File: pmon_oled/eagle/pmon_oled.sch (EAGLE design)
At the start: 37 parts, among them J1 USB, J2 USB, J4 PINHD-1X3, J5 PINHD-2X3, Q1 16Mhz, U1 LTC2943, U2 FT232RL, U3 LT1764AEQ, U4 ATMEGA328TQFP32

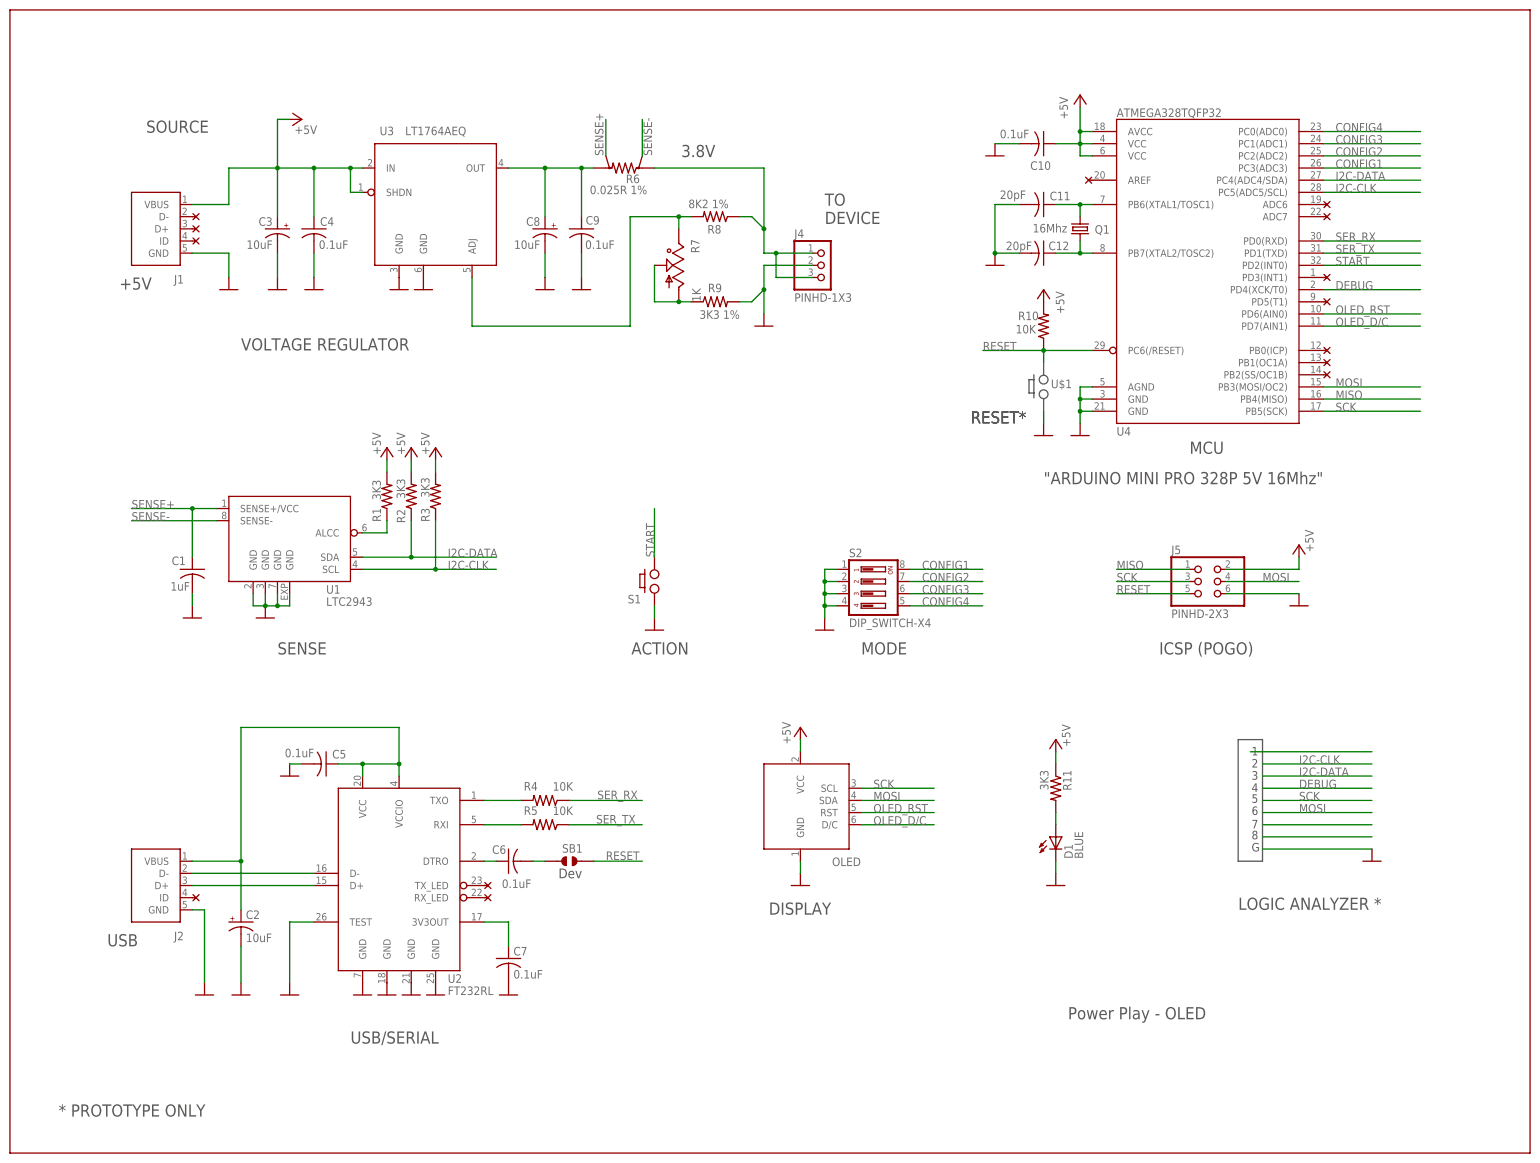
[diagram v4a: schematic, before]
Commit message: Redesigned the OLED board to pass 5V through rather than regulating to 3.8. This way it can be sued with non instrumeted devices, feeding to the USB input (with some reduce accuracy due to charger standby current and device behavior triggered by the charger in status).
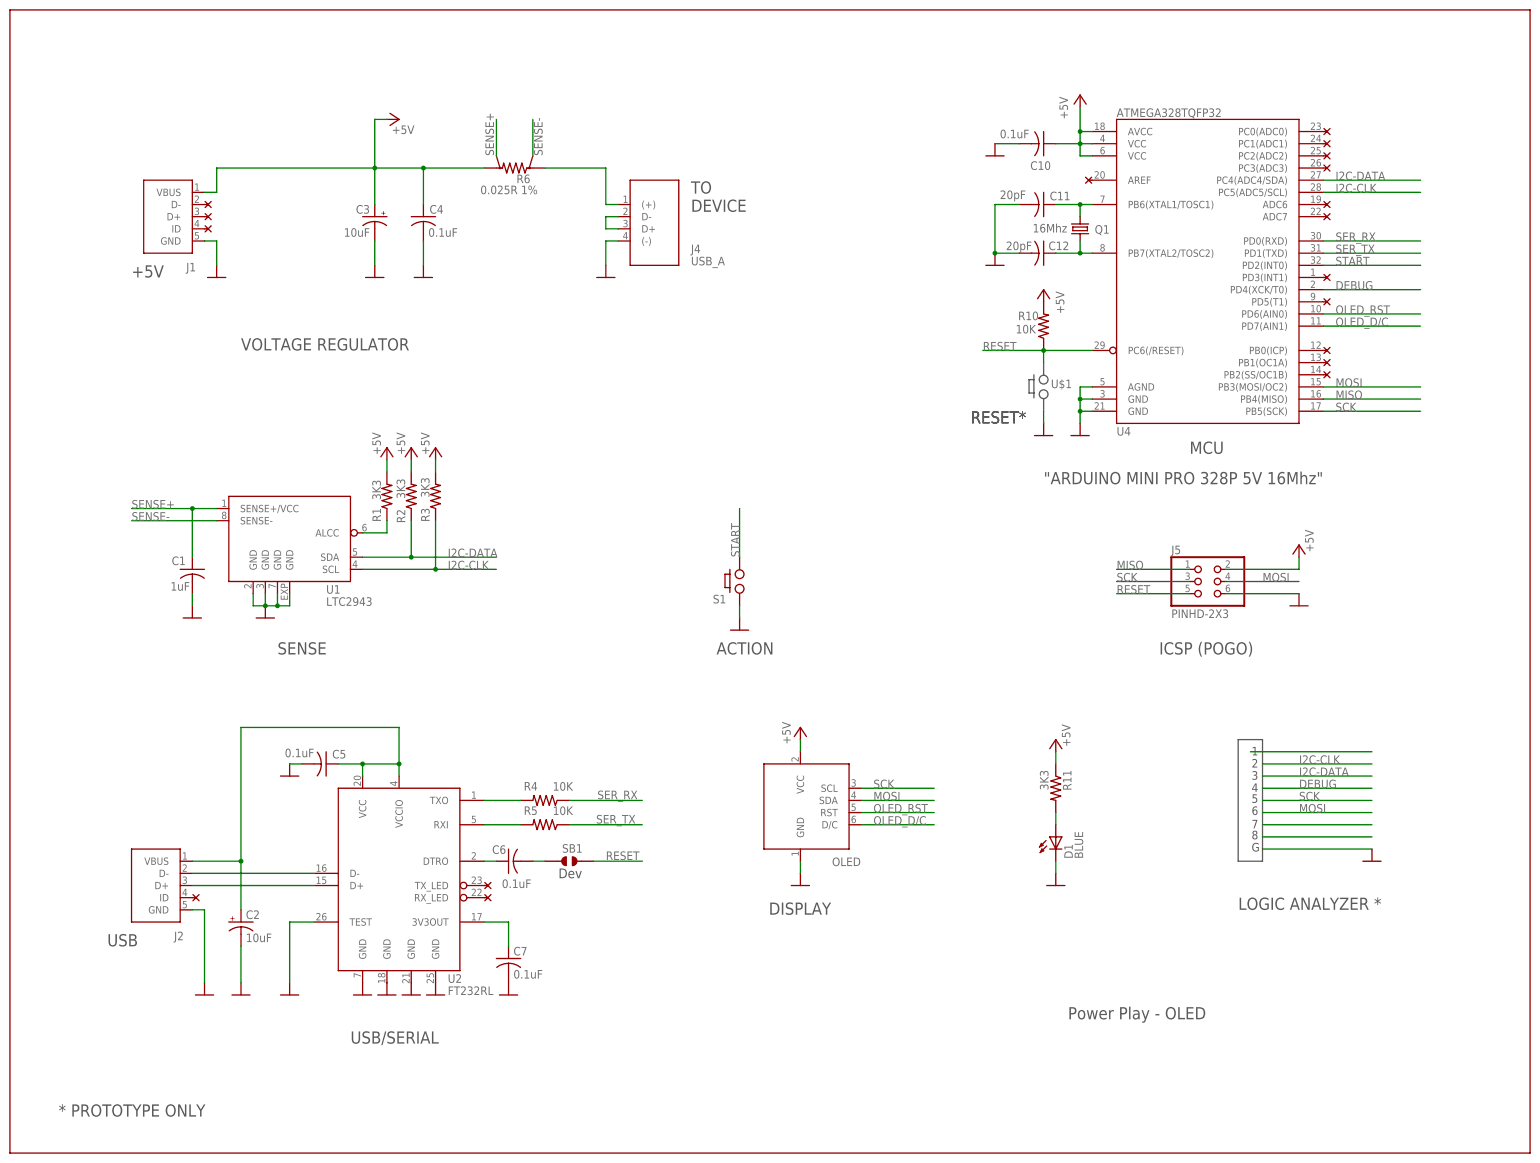
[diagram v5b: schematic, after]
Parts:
- removed C8: 10uF, pmon_oled:CPOL-USA/3216-18R
- removed C9: 0.1uF, pmon_oled:CAP-C0603
- removed R7: 1K, pmon_oled:TRIM_US-SM-42/43A
- removed R8: 8K2 1%, pmon_oled:RES-R0603
- removed R9: 3K3 1%, pmon_oled:RES-R0603
- removed S2: DIP_SWITCH-X4, pmon_oled:DIP_SWITCH-X4
- removed U3: LT1764AEQ, pmon_oled:LTE1764
- J4: value PINHD-1X3 -> USB_A; device pmon_oled:PINHD-1X3 -> pmon_oled:USB_A
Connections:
- removed net CONFIG1: S2.8, U4.PC3(ADC3)
- removed net CONFIG2: S2.7, U4.PC2(ADC2)
- removed net CONFIG3: S2.6, U4.PC1(ADC1)
- removed net CONFIG4: S2.5, U4.PC0(ADC0)
- removed net N$18: R7.1, R7.2, R9.1
- removed net N$19: R7.3, R8.2, U3.ADJ
- removed net N$9: C8.+, C9.1, R6.I2, U3.OUT
- new net N$4: J4.D+, J4.D-
- net +5V: now also R6.I2; no longer U3.IN, U3.SHDN
- net GND: now also J4.(-); no longer C8.-, C9.2, J4.2, R9.2, S2.1, S2.2, S2.3, S2.4, U3.GND@1, U3.GND@2
- net N$22: now also J4.(+); no longer J4.1, J4.3, R8.1
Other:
- note removed: "3.8V"
- note removed: "MODE"
- note removed: "SOURCE"
- moved on the sheet: C3, C4, J1, R6, S1

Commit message: Restoring the pmon_oled design with 3.8V regulator.
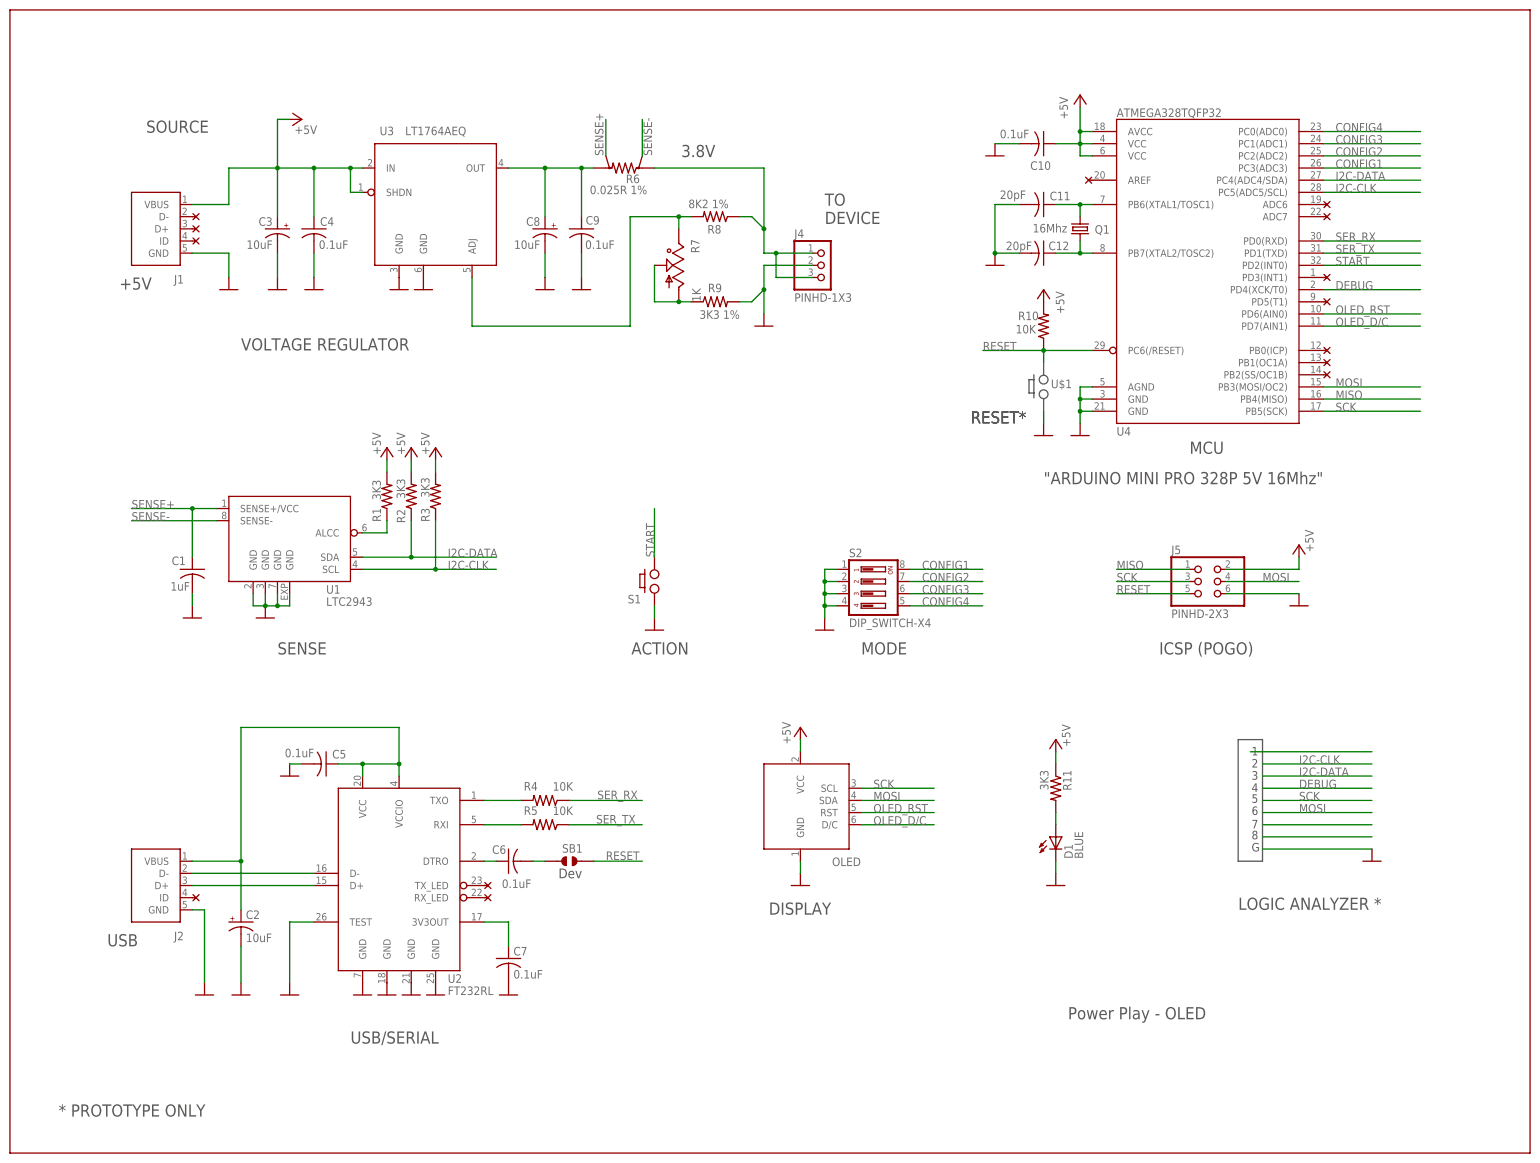
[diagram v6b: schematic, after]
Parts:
- added C8: 10uF, pmon_oled:CPOL-USA/3216-18R
- added C9: 0.1uF, pmon_oled:CAP-C0603
- added R7: 1K, pmon_oled:TRIM_US-SM-42/43A
- added R8: 8K2 1%, pmon_oled:RES-R0603
- added R9: 3K3 1%, pmon_oled:RES-R0603
- added S2: DIP_SWITCH-X4, pmon_oled:DIP_SWITCH-X4
- added U3: LT1764AEQ, pmon_oled:LTE1764
- J4: value USB_A -> PINHD-1X3; device pmon_oled:USB_A -> pmon_oled:PINHD-1X3
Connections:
- removed net N$4: J4.D+, J4.D-
- new net CONFIG1: S2.8, U4.PC3(ADC3)
- new net CONFIG2: S2.7, U4.PC2(ADC2)
- new net CONFIG3: S2.6, U4.PC1(ADC1)
- new net CONFIG4: S2.5, U4.PC0(ADC0)
- new net N$18: R7.1, R7.2, R9.1
- new net N$19: R7.3, R8.2, U3.ADJ
- new net N$9: C8.+, C9.1, R6.I2, U3.OUT
- net +5V: now also U3.IN, U3.SHDN; no longer R6.I2
- net GND: now also C8.-, C9.2, J4.2, R9.2, S2.1, S2.2, S2.3, S2.4, U3.GND@1, U3.GND@2; no longer J4.(-)
- net N$22: now also J4.1, J4.3, R8.1; no longer J4.(+)
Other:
- note added: "3.8V"
- note added: "MODE"
- note added: "SOURCE"
- moved on the sheet: C3, C4, J1, R6, S1
